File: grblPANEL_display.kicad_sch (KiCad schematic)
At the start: 13 parts, among them J501 ILI9488, Q501 Q_NPN_BEC - S8050

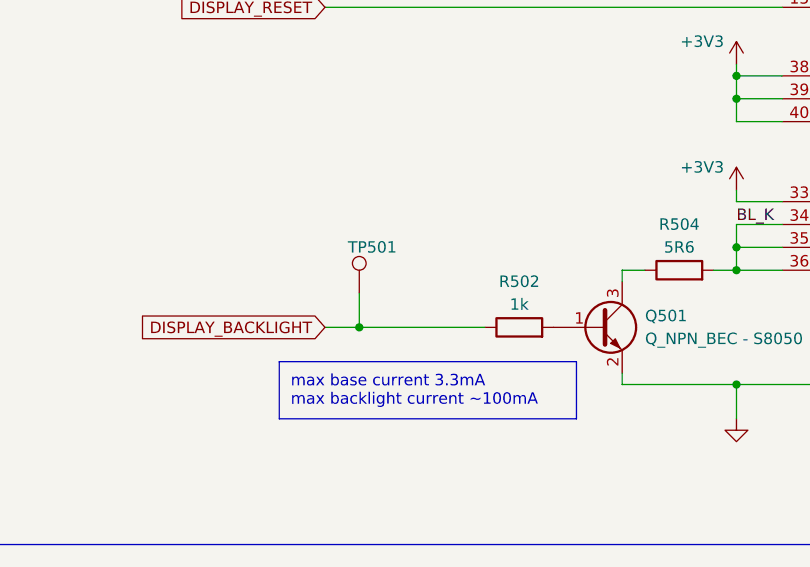
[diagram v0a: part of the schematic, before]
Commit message: Board changes for Rev B
Import changes from schematic.

Place and route changes from schematic:
Headers for serial console.
DNP components to v7 format.
Power status components.
LEDs to bottom side, plus silkscreen.

Update schematic page settings (RevB).

Update PCB page settings (RevB).

Silkscreen & test point tweaks.
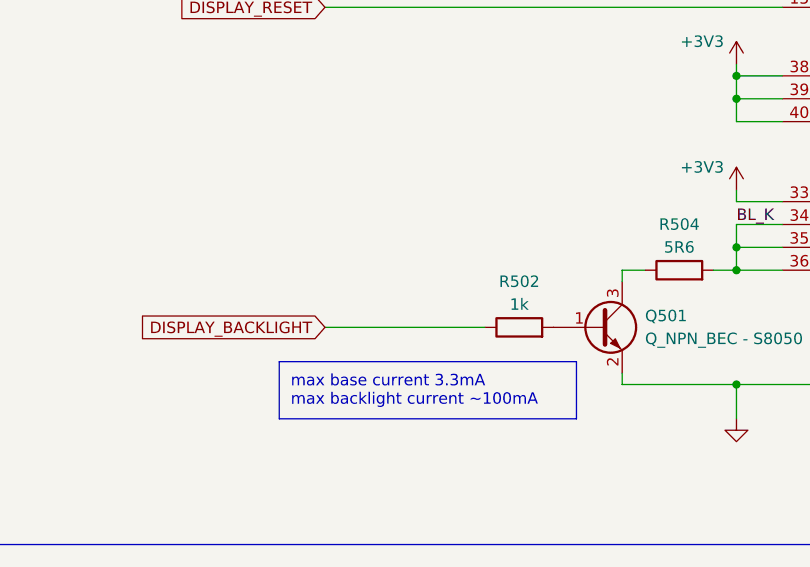
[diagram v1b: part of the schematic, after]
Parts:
- removed TP501: TestPoint, TestPoint:TestPoint_THTPad_D2.0mm_Drill1.0mm, symbol Connector:TestPoint
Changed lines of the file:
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@@
     (title "grblPANEL")
     (date "2022-12-12")
-    (rev "0.1")
+    (rev "B")
     (company "dresco")
   )
@@
   )
   (junction (at 209.55 116.84) (diameter 0) (color 0 0 0 0)
-  )
-  (junction (at 120.65 125.73) (diameter 0) (color 0 0 0 0)
   )
   (junction (at 179.07 125.73) (diameter 0) (color 0 0 0 0)
@@
     (stroke (width 0) (type default))
   )
-  (wire (pts (xy 120.65 125.73) (xy 134.62 125.73))
-    (stroke (width 0) (type default))
-  )
   (wire (pts (xy 149.86 130.81) (xy 149.86 132.08))
     (stroke (width 0) (type default))
@@
     (stroke (width 0) (type default))
   )
-  (wire (pts (xy 116.84 125.73) (xy 120.65 125.73))
+  (wire (pts (xy 116.84 125.73) (xy 134.62 125.73))
     (stroke (width 0) (type default))
   )
@@
   )
   (wire (pts (xy 203.2 114.3) (xy 209.55 114.3))
-    (stroke (width 0) (type default))
-  )
-  (wire (pts (xy 120.65 121.92) (xy 120.65 125.73))
     (stroke (width 0) (type default))
   )
@@
         )
       )
-    )
-  )
-  (symbol (lib_id "Connector:TestPoint") (at 120.65 121.92 0) (unit 1)
-    (in_bom yes) (on_board yes) (dnp no)
-    (property "Reference" "TP501" (at 119.38 116.84 0)
-      (effects (font (size 1.27 1.27)) (justify left))
-    )
-    (property "Value" "TestPoint" (at 123.19 119.8879 0)
-      (effects (font (size 1.27 1.27)) (justify left) hide)
-    )
-    (property "Footprint" "TestPoint:TestPoint_THTPad_D2.0mm_Drill1.0mm" (at 125.73 121.92 0)
-      (effects (font (size 1.27 1.27)) hide)
-    )
-    (property "Datasheet" "~" (at 125.73 121.92 0)
-      (effects (font (size 1.27 1.27)) hide)
-    )
-    (pin "1")
-    (instances
-      (project "grblPANEL"
-        (path "/1f77927e-2ca9-4002-a421-c6796d5f0016/2c60fe6e-45f9-484b-a2a4-9c1dd728d5af"
-          (reference "TP501") (unit 1)
-        )
-      )
